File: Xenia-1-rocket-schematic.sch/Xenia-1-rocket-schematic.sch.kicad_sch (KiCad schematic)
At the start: 9 parts

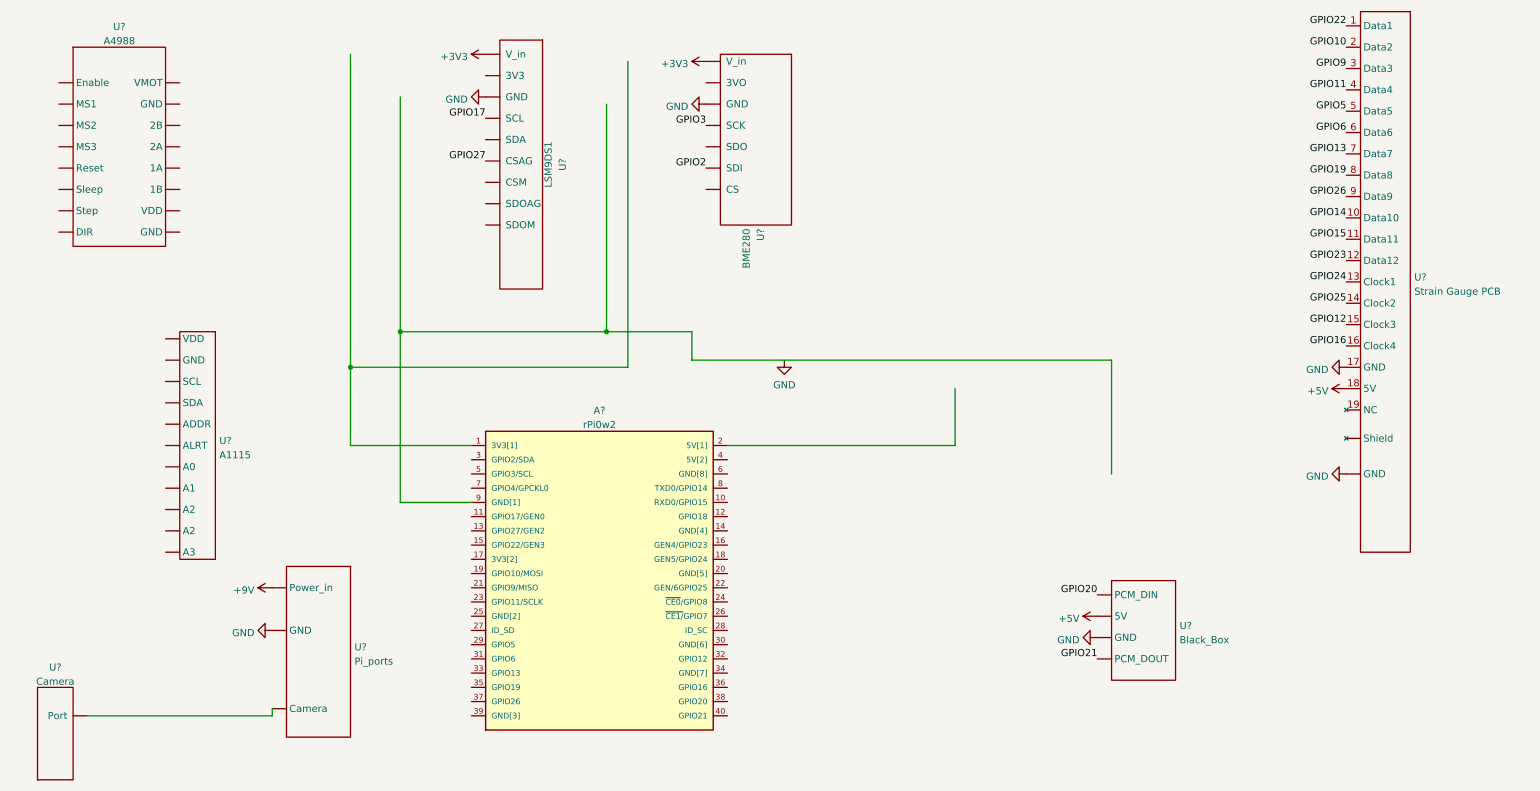
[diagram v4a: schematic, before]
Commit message: Updated the schematic
The motor controller has been wired, SDA pin on IMU changed, and a stepper motor has been added
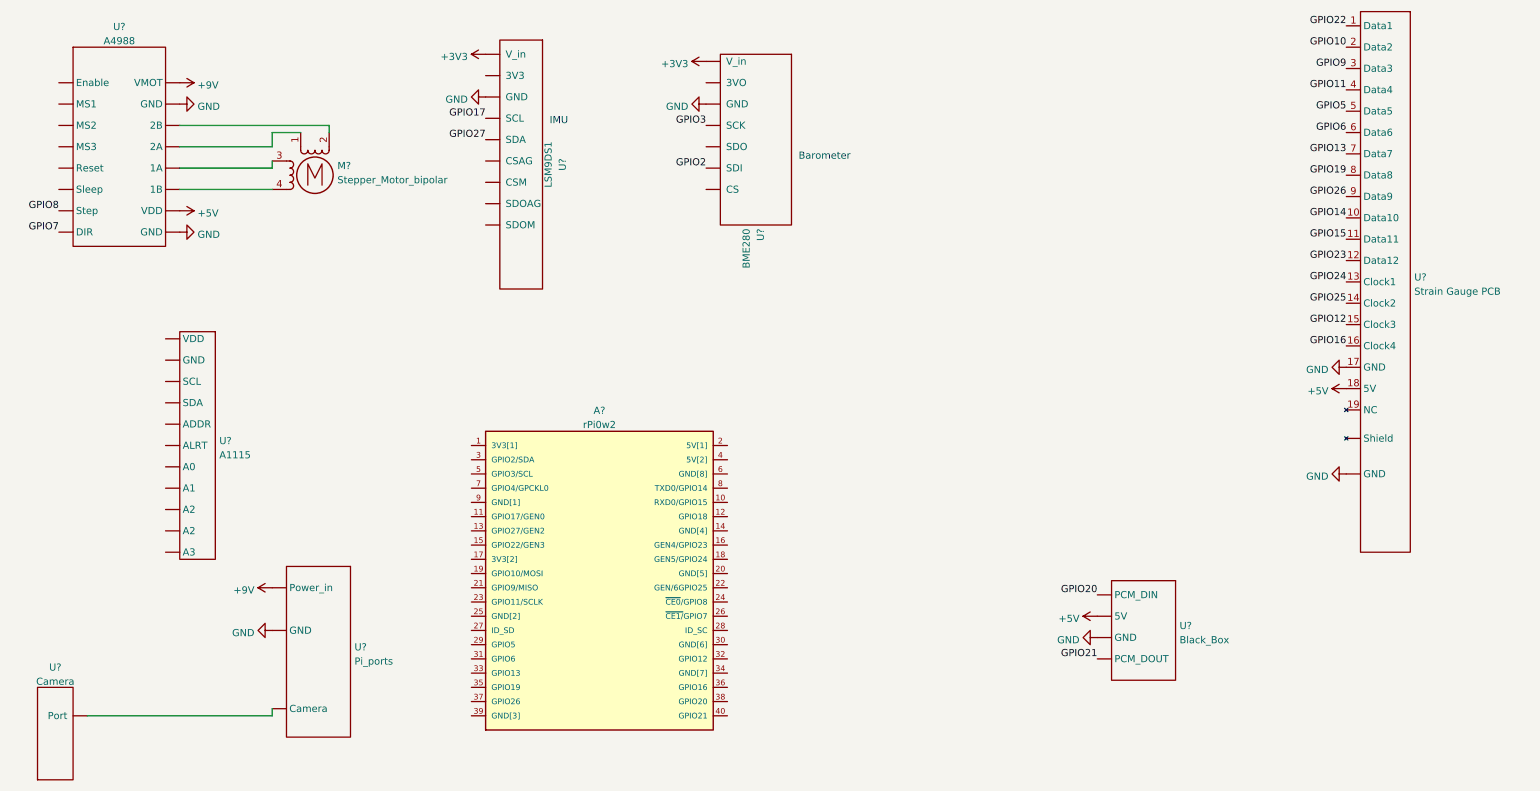
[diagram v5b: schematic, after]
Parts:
- added M?: Stepper_Motor_bipolar, symbol Motor:Stepper_Motor_bipolar
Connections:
- net +5V: now also U?. (VMOT)
- net +9V: now also U?. (VMOT)
- net GND: now also U?. (VMOT)
- net GPIO8: now reaches U?. (VMOT)
- new net: M?.1, U?. (VMOT)
- new net: M?.2 (-), U?. (VMOT)
- new net: M?.3, U?. (VMOT)
- new net: M?.4, U?. (VMOT)
- new net GPIO7: U?. (VMOT)
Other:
- note added: "Barometer"
- note added: "IMU"
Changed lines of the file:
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@@
 (kicad_sch (version 20211123) (generator eeschema)
   (paper "A4")
-  (junction (at 119.38 71.12) (diameter 0) (color 0 0 0 0)
-  )
-  (junction (at 73.66 77.47) (diameter 0) (color 0 0 0 0)
-  )
-  (junction (at 82.55 71.12) (diameter 0) (color 0 0 0 0)
-  )
   (wire (pts (xy 59.69 139.7) (xy 59.69 138.43))
     (stroke (width 0) (type default) (color 0 0 0 0))
   )
-  (wire (pts (xy 119.38 30.48) (xy 119.38 71.12))
+  (wire (pts (xy 69.85 34.29) (xy 69.85 35.56))
     (stroke (width 0) (type default) (color 0 0 0 0))
   )
@@
     (stroke (width 0) (type default) (color 0 0 0 0))
   )
-  (wire (pts (xy 181.61 81.28) (xy 181.61 91.44))
-    (stroke (width 0) (type default) (color 0 0 0 0))
-  )
-  (wire (pts (xy 134.62 76.2) (xy 134.62 71.12))
-    (stroke (width 0) (type default) (color 0 0 0 0))
-  )
-  (wire (pts (xy 82.55 29.21) (xy 82.55 71.12))
-    (stroke (width 0) (type default) (color 0 0 0 0))
-  )
-  (wire (pts (xy 73.66 77.47) (xy 73.66 91.44))
-    (stroke (width 0) (type default) (color 0 0 0 0))
-  )
-  (wire (pts (xy 82.55 71.12) (xy 119.38 71.12))
-    (stroke (width 0) (type default) (color 0 0 0 0))
-  )
-  (wire (pts (xy 82.55 71.12) (xy 82.55 101.6))
-    (stroke (width 0) (type default) (color 0 0 0 0))
-  )
-  (wire (pts (xy 209.55 96.52) (xy 209.55 76.2))
-    (stroke (width 0) (type default) (color 0 0 0 0))
-  )
-  (wire (pts (xy 123.19 77.47) (xy 73.66 77.47))
-    (stroke (width 0) (type default) (color 0 0 0 0))
-  )
-  (wire (pts (xy 123.19 22.86) (xy 123.19 77.47))
-    (stroke (width 0) (type default) (color 0 0 0 0))
-  )
-  (wire (pts (xy 73.66 21.59) (xy 73.66 77.47))
-    (stroke (width 0) (type default) (color 0 0 0 0))
-  )
-  (wire (pts (xy 134.62 71.12) (xy 119.38 71.12))
-    (stroke (width 0) (type default) (color 0 0 0 0))
-  )
-  (wire (pts (xy 209.55 76.2) (xy 134.62 76.2))
-    (stroke (width 0) (type default) (color 0 0 0 0))
-  )
-  (wire (pts (xy 82.55 101.6) (xy 95.25 101.6))
-    (stroke (width 0) (type default) (color 0 0 0 0))
-  )
-  (wire (pts (xy 181.61 91.44) (xy 140.97 91.44))
-    (stroke (width 0) (type default) (color 0 0 0 0))
-  )
-  (wire (pts (xy 73.66 91.44) (xy 95.25 91.44))
-    (stroke (width 0) (type default) (color 0 0 0 0))
+  (wire (pts (xy 43.18 45.72) (xy 59.69 45.72))
+    (stroke (width 0) (type default) (color 0 0 0 0))
+  )
+  (wire (pts (xy 59.69 35.56) (xy 59.69 38.1))
+    (stroke (width 0) (type default) (color 0 0 0 0))
+  )
+  (wire (pts (xy 64.77 35.56) (xy 59.69 35.56))
+    (stroke (width 0) (type default) (color 0 0 0 0))
+  )
+  (wire (pts (xy 43.18 34.29) (xy 69.85 34.29))
+    (stroke (width 0) (type default) (color 0 0 0 0))
+  )
+  (wire (pts (xy 43.18 41.91) (xy 59.69 41.91))
+    (stroke (width 0) (type default) (color 0 0 0 0))
+  )
+  (wire (pts (xy 43.18 38.1) (xy 59.69 38.1))
+    (stroke (width 0) (type default) (color 0 0 0 0))
+  )
+  (wire (pts (xy 59.69 41.91) (xy 59.69 40.64))
+    (stroke (width 0) (type default) (color 0 0 0 0))
+  )
+  (text "IMU" (at 109.22 34.29 0)
+    (effects (font (size 1.27 1.27)) (justify left bottom))
+  )
+  (text "Barometer" (at 153.67 40.64 0)
+    (effects (font (size 1.27 1.27)) (justify left bottom))
   )
   (label "GPIO13" (at 251.46 39.37 180)
@@
     (effects (font (size 1.27 1.27)) (justify right bottom))
   )
+  (label "GPIO27" (at 97.79 36.83 180)
+    (effects (font (size 1.27 1.27)) (justify right bottom))
+  )
   (label "GPIO15" (at 251.46 54.61 180)
     (effects (font (size 1.27 1.27)) (justify right bottom))
@@
     (effects (font (size 1.27 1.27)) (justify right bottom))
   )
+  (label "GPIO8" (at 21.59 49.53 180)
+    (effects (font (size 1.27 1.27)) (justify right bottom))
+  )
   (label "GPIO19" (at 251.46 43.18 180)
     (effects (font (size 1.27 1.27)) (justify right bottom))
@@
     (effects (font (size 1.27 1.27)) (justify right bottom))
   )
-  (label "GPIO27" (at 97.79 40.64 180)
-    (effects (font (size 1.27 1.27)) (justify right bottom))
-  )
   (label "GPIO5" (at 251.46 31.75 180)
+    (effects (font (size 1.27 1.27)) (justify right bottom))
+  )
+  (label "GPIO7" (at 21.59 53.34 180)
     (effects (font (size 1.27 1.27)) (justify right bottom))
   )
@@
     (pin "1")
   )
-  (symbol (lib_id "power:GND") (at 151.13 76.2 0) (unit 1)
-    (in_bom yes) (on_board yes) (fields_autoplaced)
-    (property "Reference" "#PWR?" (id 0) (at 151.13 82.55 0)
-      (effects (font (size 1.27 1.27)) hide)
-    )
-    (property "Value" "GND" (id 1) (at 151.13 80.6434 0))
-    (property "Footprint" "" (id 2) (at 151.13 76.2 0)
-      (effects (font (size 1.27 1.27)) hide)
-    )
-    (property "Datasheet" "" (id 3) (at 151.13 76.2 0)
+  (symbol (lib_id "power:+9V") (at 43.18 26.67 270) (unit 1)
+    (in_bom yes) (on_board yes) (fields_autoplaced)
+    (property "Reference" "#PWR?" (id 0) (at 39.37 26.67 0)
+      (effects (font (size 1.27 1.27)) hide)
+    )
+    (property "Value" "+9V" (id 1) (at 46.355 27.1038 90)
+      (effects (font (size 1.27 1.27)) (justify left))
+    )
+    (property "Footprint" "" (id 2) (at 43.18 26.67 0)
+      (effects (font (size 1.27 1.27)) hide)
+    )
+    (property "Datasheet" "" (id 3) (at 43.18 26.67 0)
+      (effects (font (size 1.27 1.27)) hide)
+    )
+    (pin "1")
+  )
+  (symbol (lib_id "power:GND") (at 43.18 53.34 90) (unit 1)
+    (in_bom yes) (on_board yes) (fields_autoplaced)
+    (property "Reference" "#PWR?" (id 0) (at 49.53 53.34 0)
+      (effects (font (size 1.27 1.27)) hide)
+    )
+    (property "Value" "GND" (id 1) (at 46.355 53.7738 90)
+      (effects (font (size 1.27 1.27)) (justify right))
+    )
+    (property "Footprint" "" (id 2) (at 43.18 53.34 0)
+      (effects (font (size 1.27 1.27)) hide)
+    )
+    (property "Datasheet" "" (id 3) (at 43.18 53.34 0)
       (effects (font (size 1.27 1.27)) hide)
     )
@@
     (pin "9")
   )
+  (symbol (lib_id "power:GND") (at 43.18 30.48 90) (unit 1)
+    (in_bom yes) (on_board yes) (fields_autoplaced)
+    (property "Reference" "#PWR?" (id 0) (at 49.53 30.48 0)
+      (effects (font (size 1.27 1.27)) hide)
+    )
+    (property "Value" "GND" (id 1) (at 46.355 30.9138 90)
+      (effects (font (size 1.27 1.27)) (justify right))
+    )
+    (property "Footprint" "" (id 2) (at 43.18 30.48 0)
+      (effects (font (size 1.27 1.27)) hide)
+    )
+    (property "Datasheet" "" (id 3) (at 43.18 30.48 0)
+      (effects (font (size 1.27 1.27)) hide)
+    )
+    (pin "1")
+  )
   (symbol (lib_id "power:+5V") (at 207.01 121.92 90) (unit 1)
     (in_bom yes) (on_board yes) (fields_autoplaced)
@@
     (pin "~")
   )
+  (symbol (lib_id "power:+5V") (at 43.18 49.53 270) (unit 1)
+    (in_bom yes) (on_board yes) (fields_autoplaced)
+    (property "Reference" "#PWR?" (id 0) (at 39.37 49.53 0)
+      (effects (font (size 1.27 1.27)) hide)
+    )
+    (property "Value" "+5V" (id 1) (at 46.355 49.9638 90)
+      (effects (font (size 1.27 1.27)) (justify left))
+    )
+    (property "Footprint" "" (id 2) (at 43.18 49.53 0)
+      (effects (font (size 1.27 1.27)) hide)
+    )
+    (property "Datasheet" "" (id 3) (at 43.18 49.53 0)
+      (effects (font (size 1.27 1.27)) hide)
+    )
+    (pin "1")
+  )
   (symbol (lib_id "power:GND") (at 59.69 124.46 270) (unit 1)
     (in_bom yes) (on_board yes) (fields_autoplaced)
@@
     )
     (pin "1")
+  )
+  (symbol (lib_id "Motor:Stepper_Motor_bipolar") (at 67.31 43.18 0) (unit 1)
+    (in_bom yes) (on_board yes) (fields_autoplaced)
+    (property "Reference" "M?" (id 0) (at 71.3232 41.4944 0)
+      (effects (font (size 1.27 1.27)) (justify left))
+    )
+    (property "Value" "Stepper_Motor_bipolar" (id 1) (at 71.3232 44.0313 0)
+      (effects (font (size 1.27 1.27)) (justify left))
+    )
+    (property "Footprint" "" (id 2) (at 67.564 43.434 0)
+      (effects (font (size 1.27 1.27)) hide)
+    )
+    (property "Datasheet" "http://www.infineon.com/dgdl/Application-Note-TLE8110EE_driving_UniPolarStepperMotor_V1.1.pdf?fileId=db3a30431be39b97011be5d0aa0a00b0" (id 3) (at 67.564 43.434 0)
+      (effects (font (size 1.27 1.27)) hide)
+    )
+    (pin "1")
+    (pin "2")
+    (pin "3")
+    (pin "4")
   )
   (sheet_instances
@@
       (reference "#PWR?") (unit 1) (value "GND") (footprint "")
     )
-    (path "/458cdc62-e3c9-4c6b-a506-564e5e44cc1c"
+    (path "/21e46ce2-bf6c-43c1-9fdf-ca7848b8cb0f"
+      (reference "#PWR?") (unit 1) (value "+9V") (footprint "")
+    )
+    (path "/30eee620-3019-4051-bbd1-72b9b7ab7e2c"
       (reference "#PWR?") (unit 1) (value "GND") (footprint "")
     )
@@
       (reference "#PWR?") (unit 1) (value "+3V3") (footprint "")
     )
+    (path "/69143909-70ed-4bd9-82fc-2a9640e1097b"
+      (reference "#PWR?") (unit 1) (value "GND") (footprint "")
+    )
     (path "/714dbc41-6191-41b3-84ec-f507b98f0f50"
       (reference "#PWR?") (unit 1) (value "+5V") (footprint "")
@@
       (reference "#PWR?") (unit 1) (value "+5V") (footprint "")
     )
+    (path "/c95c521c-4576-4c70-90ba-c66ad835a68e"
+      (reference "#PWR?") (unit 1) (value "+5V") (footprint "")
+    )
     (path "/d456e6f9-b0b3-4852-93a4-f3350551011a"
       (reference "#PWR?") (unit 1) (value "GND") (footprint "")
@@
       (reference "A?") (unit 1) (value "rPi0w2") (footprint "ADA3708_RPI-ZERO")
     )
+    (path "/fe37751f-5e5d-46cf-b848-abb7dcc9ad75"
+      (reference "M?") (unit 1) (value "Stepper_Motor_bipolar") (footprint "")
+    )
     (path "/5d4dea52-a2eb-44ab-8dc5-ed93c62ecf28"

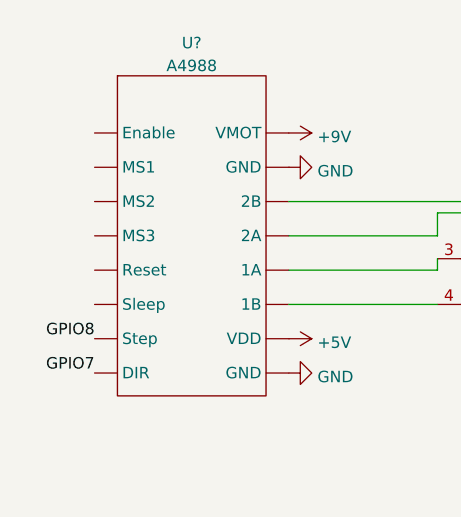
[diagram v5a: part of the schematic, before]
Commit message: Updating schematic
Connecting pins to the 5V line and adding a GPIO port allocation to the stepper motor controller.
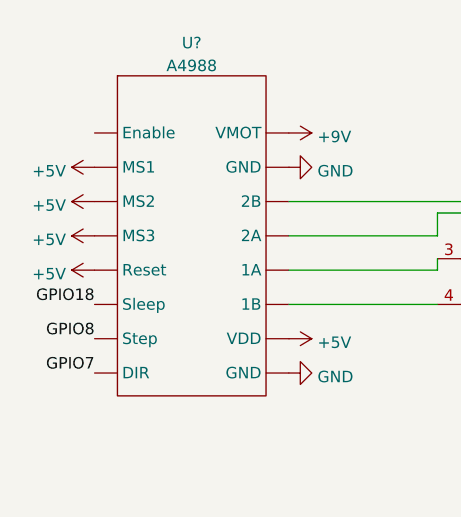
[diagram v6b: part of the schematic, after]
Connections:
- new net GPIO18: U?. (VMOT)
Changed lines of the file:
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@@
+    (effects (font (size 1.27 1.27)) (justify right bottom))
+  )
+  (label "GPIO18" (at 21.59 45.72 180)
     (effects (font (size 1.27 1.27)) (justify right bottom))
   )
@@
     (pin "1")
   )
+  (symbol (lib_id "power:+5V") (at 21.59 38.1 90) (unit 1)
+    (in_bom yes) (on_board yes) (fields_autoplaced)
+    (property "Reference" "#PWR?" (id 0) (at 25.4 38.1 0)
+      (effects (font (size 1.27 1.27)) hide)
+    )
+    (property "Value" "+5V" (id 1) (at 18.4151 38.5338 90)
+      (effects (font (size 1.27 1.27)) (justify left))
+    )
+    (property "Footprint" "" (id 2) (at 21.59 38.1 0)
+      (effects (font (size 1.27 1.27)) hide)
+    )
+    (property "Datasheet" "" (id 3) (at 21.59 38.1 0)
+      (effects (font (size 1.27 1.27)) hide)
+    )
+    (pin "1")
+  )
+  (symbol (lib_id "power:+5V") (at 21.59 34.29 90) (unit 1)
+    (in_bom yes) (on_board yes) (fields_autoplaced)
+    (property "Reference" "#PWR?" (id 0) (at 25.4 34.29 0)
+      (effects (font (size 1.27 1.27)) hide)
+    )
+    (property "Value" "+5V" (id 1) (at 18.4151 34.7238 90)
+      (effects (font (size 1.27 1.27)) (justify left))
+    )
+    (property "Footprint" "" (id 2) (at 21.59 34.29 0)
+      (effects (font (size 1.27 1.27)) hide)
+    )
+    (property "Datasheet" "" (id 3) (at 21.59 34.29 0)
+      (effects (font (size 1.27 1.27)) hide)
+    )
+    (pin "1")
+  )
   (symbol (lib_id "power:+9V") (at 43.18 26.67 270) (unit 1)
     (in_bom yes) (on_board yes) (fields_autoplaced)
@@
     (pin "")
   )
+  (symbol (lib_id "power:+5V") (at 21.59 41.91 90) (unit 1)
+    (in_bom yes) (on_board yes) (fields_autoplaced)
+    (property "Reference" "#PWR?" (id 0) (at 25.4 41.91 0)
+      (effects (font (size 1.27 1.27)) hide)
+    )
+    (property "Value" "+5V" (id 1) (at 18.4151 42.3438 90)
+      (effects (font (size 1.27 1.27)) (justify left))
+    )
+    (property "Footprint" "" (id 2) (at 21.59 41.91 0)
+      (effects (font (size 1.27 1.27)) hide)
+    )
+    (property "Datasheet" "" (id 3) (at 21.59 41.91 0)
+      (effects (font (size 1.27 1.27)) hide)
+    )
+    (pin "1")
+  )
   (symbol (lib_id "power:+5V") (at 251.46 81.28 90) (unit 1)
     (in_bom yes) (on_board yes) (fields_autoplaced)
@@
     (pin "1")
   )
+  (symbol (lib_id "power:+5V") (at 21.59 30.48 90) (unit 1)
+    (in_bom yes) (on_board yes) (fields_autoplaced)
+    (property "Reference" "#PWR?" (id 0) (at 25.4 30.48 0)
+      (effects (font (size 1.27 1.27)) hide)
+    )
+    (property "Value" "+5V" (id 1) (at 18.4151 30.9138 90)
+      (effects (font (size 1.27 1.27)) (justify left))
+    )
+    (property "Footprint" "" (id 2) (at 21.59 30.48 0)
+      (effects (font (size 1.27 1.27)) hide)
+    )
+    (property "Datasheet" "" (id 3) (at 21.59 30.48 0)
+      (effects (font (size 1.27 1.27)) hide)
+    )
+    (pin "1")
+  )
   (symbol (lib_id "power:GND") (at 251.46 96.52 270) (unit 1)
     (in_bom yes) (on_board yes) (fields_autoplaced)
@@
       (reference "#PWR?") (unit 1) (value "GND") (footprint "")
     )
+    (path "/1b61a6f3-224e-4630-807e-b1df72a82aa5"
+      (reference "#PWR?") (unit 1) (value "+5V") (footprint "")
+    )
+    (path "/20b6b7c7-49ab-407c-841c-3a8dfb05c717"
+      (reference "#PWR?") (unit 1) (value "+5V") (footprint "")
+    )
     (path "/21e46ce2-bf6c-43c1-9fdf-ca7848b8cb0f"
       (reference "#PWR?") (unit 1) (value "+9V") (footprint "")
@@
       (reference "#PWR?") (unit 1) (value "+3V3") (footprint "")
     )
+    (path "/a77e7da7-f5c3-4818-8c15-0227f072e451"
+      (reference "#PWR?") (unit 1) (value "+5V") (footprint "")
+    )
     (path "/b654340b-e22a-4629-b9dc-82da6676aa13"
       (reference "#PWR?") (unit 1) (value "+5V") (footprint "")
@@
       (reference "#PWR?") (unit 1) (value "GND") (footprint "")
     )
+    (path "/f3c4d7e7-c55c-4985-8812-602443bead0e"
+      (reference "#PWR?") (unit 1) (value "+5V") (footprint "")
+    )
     (path "/fb6e9173-28d5-4054-9860-955f43f247ce"

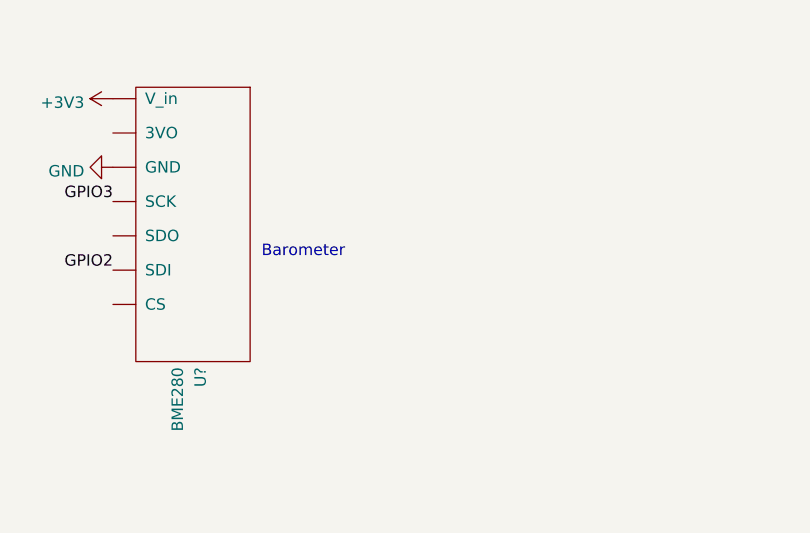
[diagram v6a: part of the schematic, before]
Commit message: Updated name on schematic
Updated Barometer to read Barometric Pressure Sensor
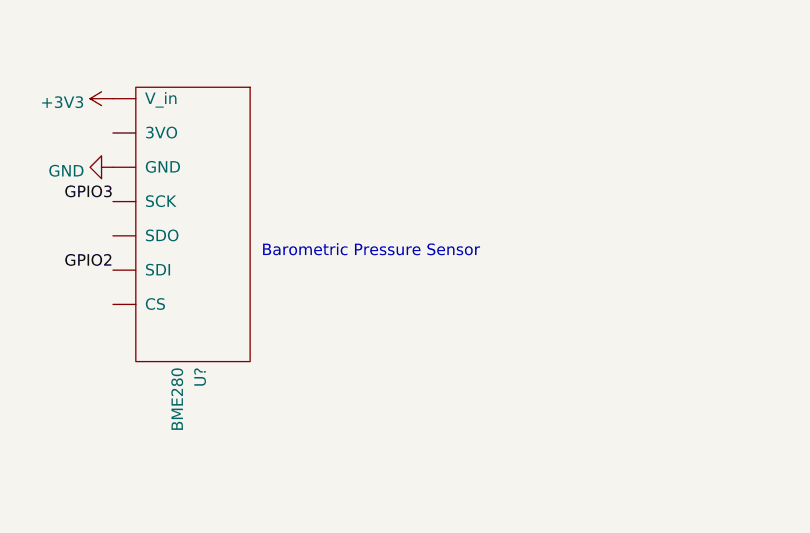
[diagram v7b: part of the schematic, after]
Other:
- note added: "Barometric Pressure Sensor"
- note removed: "Barometer"
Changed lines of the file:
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@@
     (effects (font (size 1.27 1.27)) (justify left bottom))
   )
-  (text "Barometer" (at 153.67 40.64 0)
+  (text "Barometric Pressure Sensor" (at 153.67 40.64 0)
     (effects (font (size 1.27 1.27)) (justify left bottom))
   )
